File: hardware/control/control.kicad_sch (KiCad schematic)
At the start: 58 parts, among them J1 Conn_01x05_Male, J2 CANPWR, J3 CANGND, J4 RJ45, J5 RJ45, J6 Conn_02x03_Odd_Even, J7 DCDC-PWM, J8 DCDC-MEASURES, J9 display, Q1 BSS123, SW1 next, SW2 select, U1 2.048V, U2 AP63200WU, U3 PIC18F27Q84, U4 TLE9250VSJXUMA1, Y1 10Mhz

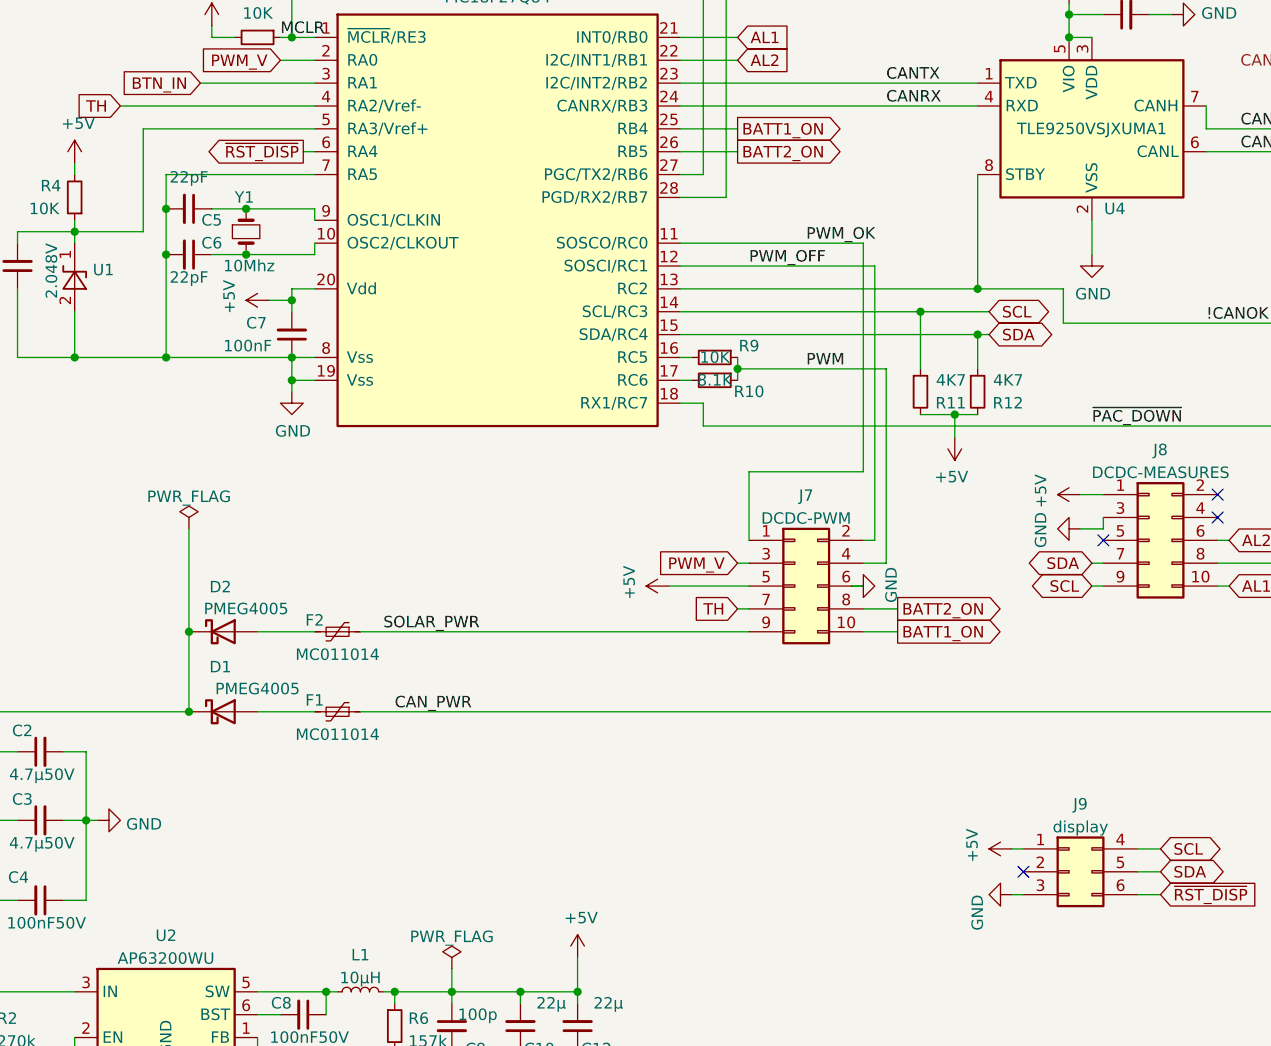
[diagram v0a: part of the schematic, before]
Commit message: Route unused RA5 to display and power board connectors, "just in case"
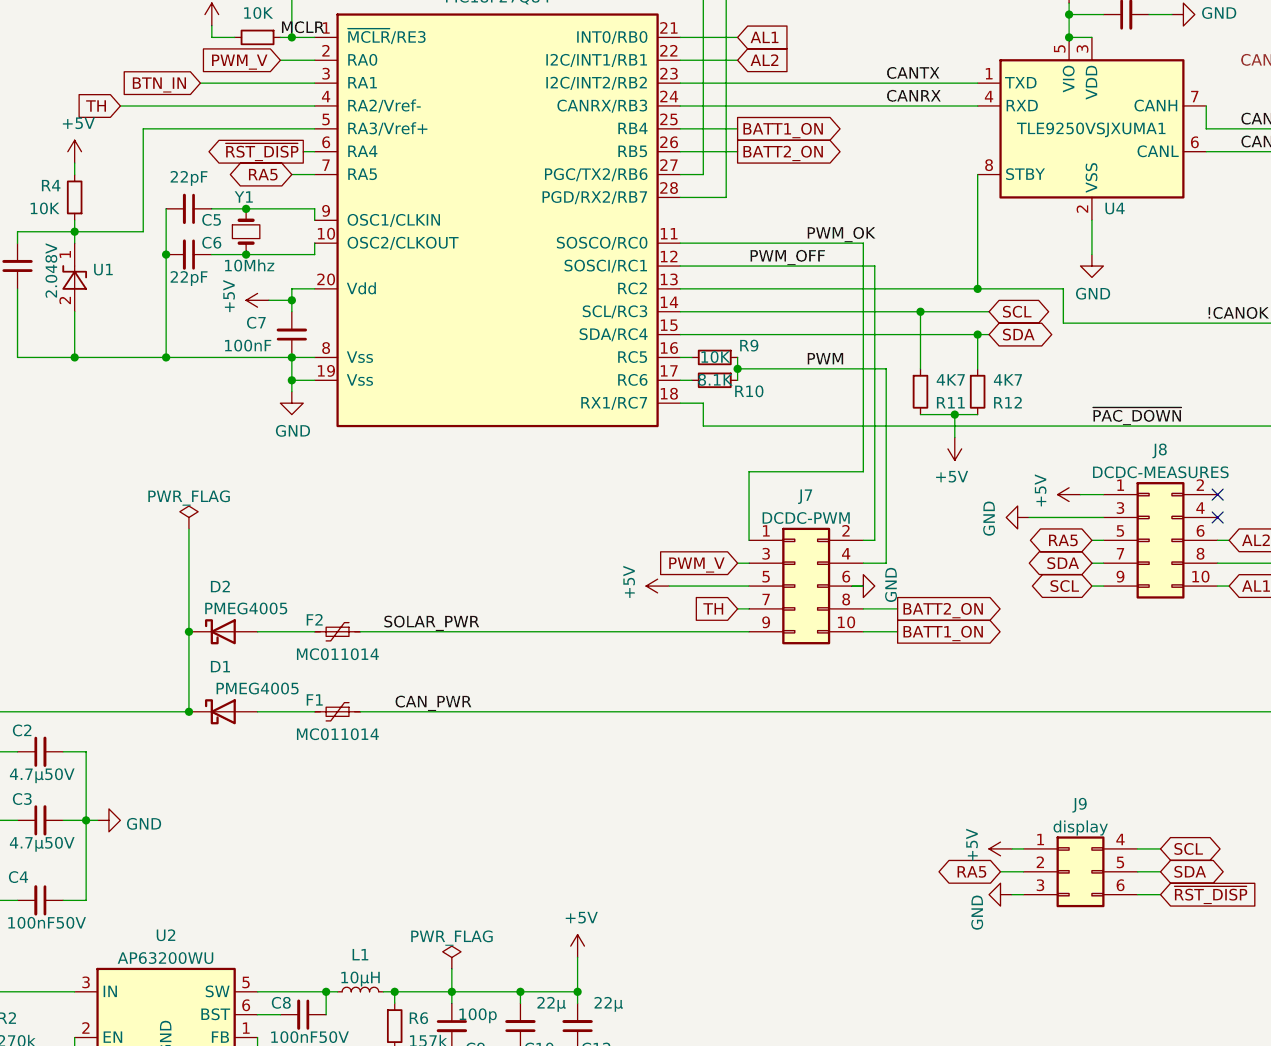
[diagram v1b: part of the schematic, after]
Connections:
- net GND: no longer U3.7 (RA5)
- net RA5: now reaches J9.2 (Pin_2)
- net RA5: now also J8.5 (Pin_5), U3.7 (RA5)
- no-connect marks 8 -> 6
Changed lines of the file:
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@@
   (junction (at 134.62 82.55) (diameter 0) (color 0 0 0 0)
   )
-  (junction (at 44.45 68.58) (diameter 0) (color 0 0 0 0)
-  )
-  (no_connect (at 148.59 105.41))
   (no_connect (at 212.09 147.32))
   (no_connect (at 201.93 147.32))
@@
   (no_connect (at 161.29 102.87))
   (no_connect (at 161.29 100.33))
-  (no_connect (at 139.7 142.24))
   (wire (pts (xy 101.6 80.01) (xy 128.27 80.01))
     (stroke (width 0) (type default) (color 0 0 0 0))
@@
     (stroke (width 0) (type default) (color 0 0 0 0))
   )
+  (wire (pts (xy 58.42 64.77) (xy 60.96 64.77))
+    (stroke (width 0) (type default) (color 0 0 0 0))
+  )
   (wire (pts (xy 255.27 67.31) (xy 259.08 67.31))
     (stroke (width 0) (type default) (color 0 0 0 0))
@@
     (stroke (width 0) (type default) (color 0 0 0 0))
   )
-  (wire (pts (xy 148.59 104.14) (xy 148.59 102.87))
-    (stroke (width 0) (type default) (color 0 0 0 0))
-  )
   (wire (pts (xy 148.59 46.99) (xy 144.78 46.99))
     (stroke (width 0) (type default) (color 0 0 0 0))
@@
     (stroke (width 0) (type default) (color 0 0 0 0))
   )
+  (wire (pts (xy 137.16 142.24) (xy 139.7 142.24))
+    (stroke (width 0) (type default) (color 0 0 0 0))
+  )
   (wire (pts (xy 90.17 155.575) (xy 90.17 156.845))
     (stroke (width 0) (type default) (color 0 0 0 0))
@@
     (stroke (width 0) (type default) (color 0 0 0 0))
   )
+  (wire (pts (xy 147.32 105.41) (xy 148.59 105.41))
+    (stroke (width 0) (type default) (color 0 0 0 0))
+  )
   (wire (pts (xy 207.01 54.61) (xy 231.14 54.61))
     (stroke (width 0) (type default) (color 0 0 0 0))
@@
     (stroke (width 0) (type default) (color 0 0 0 0))
   )
-  (wire (pts (xy 44.45 64.77) (xy 44.45 68.58))
-    (stroke (width 0) (type default) (color 0 0 0 0))
-  )
   (wire (pts (xy 144.78 46.99) (xy 144.78 49.53))
     (stroke (width 0) (type default) (color 0 0 0 0))
@@
     (stroke (width 0) (type default) (color 0 0 0 0))
   )
-  (wire (pts (xy 146.05 104.14) (xy 148.59 104.14))
+  (wire (pts (xy 140.335 102.87) (xy 148.59 102.87))
     (stroke (width 0) (type default) (color 0 0 0 0))
   )
@@
   )
   (wire (pts (xy 179.07 92.71) (xy 179.07 91.44))
-    (stroke (width 0) (type default) (color 0 0 0 0))
-  )
-  (wire (pts (xy 44.45 64.77) (xy 60.96 64.77))
     (stroke (width 0) (type default) (color 0 0 0 0))
   )
@@
     )
   )
+  (global_label "RA5" (shape tri_state) (at 58.42 64.77 180) (fields_autoplaced)
+    (effects (font (size 1.27 1.27)) (justify right))
+    (property "Intersheet References" "${INTERSHEET_REFS}" (id 0) (at 52.4388 64.6906 0)
+      (effects (font (size 1.27 1.27)) (justify right) hide)
+    )
+  )
   (global_label "~{RST_DISP}" (shape output) (at 59.69 62.23 180) (fields_autoplaced)
     (effects (font (size 1.27 1.27)) (justify right))
@@
     )
   )
+  (global_label "RA5" (shape tri_state) (at 137.16 142.24 180) (fields_autoplaced)
+    (effects (font (size 1.27 1.27)) (justify right))
+    (property "Intersheet References" "${INTERSHEET_REFS}" (id 0) (at 131.1788 142.1606 0)
+      (effects (font (size 1.27 1.27)) (justify right) hide)
+    )
+  )
   (global_label "AL2" (shape input) (at 162.56 105.41 0) (fields_autoplaced)
     (effects (font (size 1.27 1.27)) (justify left))
@@
     (effects (font (size 1.27 1.27)) (justify right))
     (property "Intersheet References" "${INTERSHEET_REFS}" (id 0) (at 103.2388 112.9506 0)
+      (effects (font (size 1.27 1.27)) (justify right) hide)
+    )
+  )
+  (global_label "RA5" (shape tri_state) (at 147.32 105.41 180) (fields_autoplaced)
+    (effects (font (size 1.27 1.27)) (justify right))
+    (property "Intersheet References" "${INTERSHEET_REFS}" (id 0) (at 141.3388 105.3306 0)
       (effects (font (size 1.27 1.27)) (justify right) hide)
     )
@@
     (pin "1")
   )
-  (symbol (lib_id "power:GND") (at 146.05 104.14 270) (unit 1)
-    (in_bom yes) (on_board yes)
-    (property "Reference" "#PWR0104" (id 0) (at 139.7 104.14 0)
-      (effects (font (size 1.27 1.27)) hide)
-    )
-    (property "Value" "GND" (id 1) (at 141.6558 104.267 0))
-    (property "Footprint" "" (id 2) (at 146.05 104.14 0)
-      (effects (font (size 1.27 1.27)) hide)
-    )
-    (property "Datasheet" "" (id 3) (at 146.05 104.14 0)
-      (effects (font (size 1.27 1.27)) hide)
-    )
+  (symbol (lib_id "power:GND") (at 140.335 102.87 270) (unit 1)
+    (in_bom yes) (on_board yes)
+    (property "Reference" "#PWR0104" (id 0) (at 133.985 102.87 0)
+      (effects (font (size 1.27 1.27)) hide)
+    )
+    (property "Value" "GND" (id 1) (at 135.9408 102.997 0))
+    (property "Footprint" "" (id 2) (at 140.335 102.87 0)
+      (effects (font (size 1.27 1.27)) hide)
+    )
+    (property "Datasheet" "" (id 3) (at 140.335 102.87 0)
+      (effects (font (size 1.27 1.27)) hide)
+    )
